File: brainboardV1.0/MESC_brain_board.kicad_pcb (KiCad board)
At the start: 4 copper layers, 90.5 x 68.6 mm, 55 parts, among them J1 Conn_01x18, J12 Conn_01x03, J13 Conn_01x03, J14 SERIAL1, J15 Conn_01x03, J22 Conn_01x01, J24 Conn_01x01, J25 Conn_01x01, Q1 my_BC337, U1 TJA1050T/CM,118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

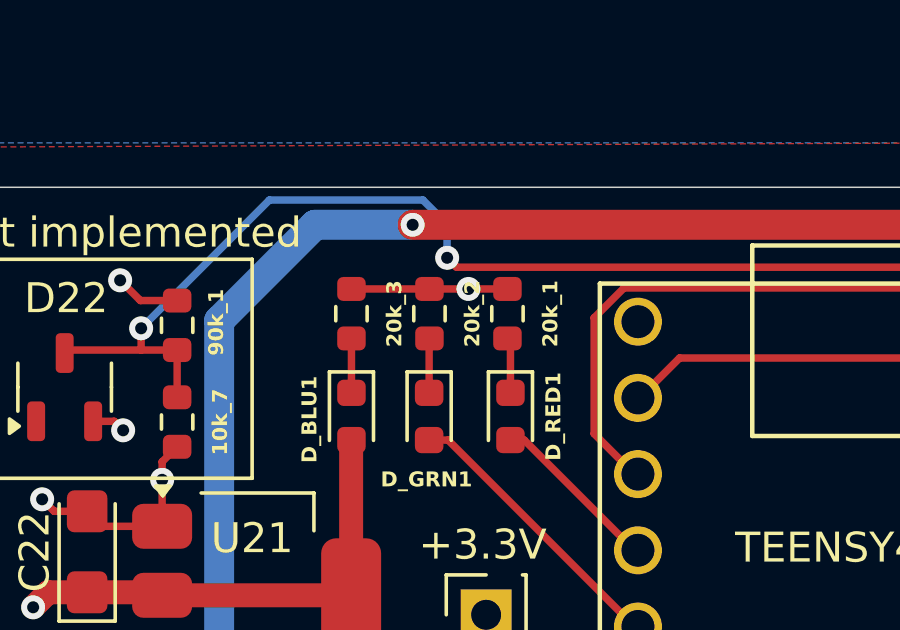
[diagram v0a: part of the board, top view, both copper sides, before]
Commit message: update grn LED resistor
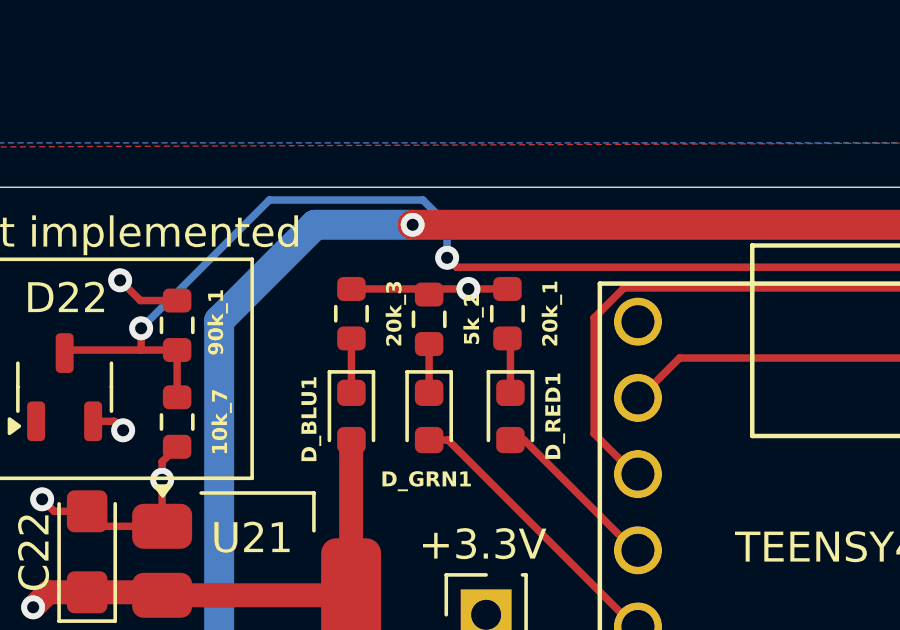
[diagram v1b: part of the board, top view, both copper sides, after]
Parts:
- removed 20k_2: 20k, Resistor_SMD:R_0603_1608Metric
- added 5k_2: 5k, Resistor_SMD:R_0603_1608Metric, F.Cu at (41.1, 19.9)
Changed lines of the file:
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@@
 		)
 	)
-	(footprint "Resistor_SMD:R_0603_1608Metric"
-		(layer "F.Cu")
-		(at 41.11 19.71375 -90)
-		(descr "Resistor SMD 0603 (1608 Metric), square (rectangular) end terminal, IPC_7351 nominal, (Body size source: IPC-SM-782 page 72, https://www.pcb-3d.com/wordpress/wp-content/uploads/ipc-sm-782a_amendment_1_and_2.pdf), generated with kicad-footprint-generator")
-		(tags "resistor")
-		(property "Reference" "20k_2"
-			(at 0 -1.43 90)
-			(layer "F.SilkS")
-			(effects
-				(font
-					(size 0.5 0.5)
-					(thickness 0.1)
-					(bold yes)
-				)
-			)
-		)
-		(property "Value" "20k"
-			(at 0 1.43 90)
-			(layer "F.Fab")
-			(effects
-				(font
-					(size 1 1)
-					(thickness 0.15)
-				)
-			)
-		)
-		(property "Footprint" "Resistor_SMD:R_0603_1608Metric"
-			(at 0 0 -90)
-			(unlocked yes)
-			(layer "F.Fab")
-			(hide yes)
-			(effects
-				(font
-					(size 1.27 1.27)
-					(thickness 0.15)
-				)
-			)
-		)
-		(property "Datasheet" ""
-			(at 0 0 -90)
-			(unlocked yes)
-			(layer "F.Fab")
-			(hide yes)
-			(effects
-				(font
-					(size 1.27 1.27)
-					(thickness 0.15)
-				)
-			)
-		)
-		(property "Description" ""
-			(at 0 0 -90)
-			(unlocked yes)
-			(layer "F.Fab")
-			(hide yes)
-			(effects
-				(font
-					(size 1.27 1.27)
-					(thickness 0.15)
-				)
-			)
-		)
-		(property "LCSC" "C4184"
-			(at 0 0 -90)
-			(unlocked yes)
-			(layer "F.Fab")
-			(hide yes)
-			(effects
-				(font
-					(size 1 1)
-					(thickness 0.15)
-				)
-			)
-		)
-		(property ki_fp_filters "R_*")
-		(sheetname "POWER Sheet")
-		(sheetfile "POWER.kicad_sch")
-		(attr smd)
-		(fp_line
-			(start -0.237258 0.5225)
-			(end 0.237258 0.5225)
-			(stroke
-				(width 0.12)
-				(type solid)
-			)
-			(layer "F.SilkS")
-		)
-		(fp_line
-			(start -0.237258 -0.5225)
-			(end 0.237258 -0.5225)
-			(stroke
-				(width 0.12)
-				(type solid)
-			)
-			(layer "F.SilkS")
-		)
-		(fp_line
-			(start -1.48 0.73)
-			(end -1.48 -0.73)
-			(stroke
-				(width 0.05)
-				(type solid)
-			)
-			(layer "F.CrtYd")
-		)
-		(fp_line
-			(start 1.48 0.73)
-			(end -1.48 0.73)
-			(stroke
-				(width 0.05)
-				(type solid)
-			)
-			(layer "F.CrtYd")
-		)
-		(fp_line
-			(start -1.48 -0.73)
-			(end 1.48 -0.73)
-			(stroke
-				(width 0.05)
-				(type solid)
-			)
-			(layer "F.CrtYd")
-		)
-		(fp_line
-			(start 1.48 -0.73)
-			(end 1.48 0.73)
-			(stroke
-				(width 0.05)
-				(type solid)
-			)
-			(layer "F.CrtYd")
-		)
-		(fp_line
-			(start -0.8 0.4125)
-			(end -0.8 -0.4125)
-			(stroke
-				(width 0.1)
-				(type solid)
-			)
-			(layer "F.Fab")
-		)
-		(fp_line
-			(start 0.8 0.4125)
-			(end -0.8 0.4125)
-			(stroke
-				(width 0.1)
-				(type solid)
-			)
-			(layer "F.Fab")
-		)
-		(fp_line
-			(start -0.8 -0.4125)
-			(end 0.8 -0.4125)
-			(stroke
-				(width 0.1)
-				(type solid)
-			)
-			(layer "F.Fab")
-		)
-		(fp_line
-			(start 0.8 -0.4125)
-			(end 0.8 0.4125)
-			(stroke
-				(width 0.1)
-				(type solid)
-			)
-			(layer "F.Fab")
-		)
-		(fp_text user "${REFERENCE}"
-			(at 0 0 90)
-			(layer "F.Fab")
-			(effects
-				(font
-					(size 0.4 0.4)
-					(thickness 0.06)
-				)
-			)
-		)
-		(pad "1" smd roundrect
-			(at -0.825 0 270)
-			(size 0.8 0.95)
-			(layers "F.Cu" "F.Paste" "F.Mask")
-			(roundrect_rratio 0.25)
-			(net 1 "GND")
-			(pintype "passive")
-		)
-		(pad "2" smd roundrect
-			(at 0.825 0 270)
-			(size 0.8 0.95)
-			(layers "F.Cu" "F.Paste" "F.Mask")
-			(roundrect_rratio 0.25)
-			(net 85 "Net-(D_GRN1-K)")
-			(pintype "passive")
-		)
-		(model "${KICAD8_3DMODEL_DIR}/Resistor_SMD.3dshapes/R_0603_1608Metric.wrl"
-			(offset
-				(xyz 0 0 0)
-			)
-			(scale
-				(xyz 1 1 1)
-			)
-			(rotate
-				(xyz 0 0 0)
-			)
-		)
-	)
 	(footprint "Converter_DCDC:my_buck_boost"
 		(layer "F.Cu")
@@
 			(offset
 				(xyz 0 0 0)
+			)
+			(scale
+				(xyz 1 1 1)
+			)
+			(rotate
+				(xyz 0 0 0)
+			)
+		)
+	)
+	(footprint "Resistor_SMD:R_0603_1608Metric"
+		(layer "F.Cu")
+		(at 41.1 19.9 -90)
+		(descr "Resistor SMD 0603 (1608 Metric), square (rectangular) end terminal, IPC_7351 nominal, (Body size source: IPC-SM-782 page 72, https://www.pcb-3d.com/wordpress/wp-content/uploads/ipc-sm-782a_amendment_1_and_2.pdf), generated with kicad-footprint-generator")
+		(tags "resistor")
+		(property "Reference" "5k_2"
+			(at 0 -1.43 90)
+			(layer "F.SilkS")
+			(effects
+				(font
+					(size 0.5 0.5)
+					(thickness 0.1)
+					(bold yes)
+				)
+			)
+		)
+		(property "Value" "5k"
+			(at 0 1.43 90)
+			(layer "F.Fab")
+			(hide yes)
+			(effects
+				(font
+					(size 1 1)
+					(thickness 0.15)
+				)
+			)
+		)
+		(property "Footprint" "Resistor_SMD:R_0603_1608Metric"
+			(at 0 0 -90)
+			(unlocked yes)
+			(layer "F.Fab")
+			(hide yes)
+			(effects
+				(font
+					(size 1.27 1.27)
+					(thickness 0.15)
+				)
+			)
+		)
+		(property "Datasheet" ""
+			(at 0 0 -90)
+			(unlocked yes)
+			(layer "F.Fab")
+			(hide yes)
+			(effects
+				(font
+					(size 1.27 1.27)
+					(thickness 0.15)
+				)
+			)
+		)
+		(property "Description" ""
+			(at 0 0 -90)
+			(unlocked yes)
+			(layer "F.Fab")
+			(hide yes)
+			(effects
+				(font
+					(size 1.27 1.27)
+					(thickness 0.15)
+				)
+			)
+		)
+		(property "LCSC" "C4184"
+			(at 0 0 -90)
+			(unlocked yes)
+			(layer "F.Fab")
+			(hide yes)
+			(effects
+				(font
+					(size 1 1)
+					(thickness 0.15)
+				)
+			)
+		)
+		(property ki_fp_filters "R_*")
+		(sheetname "POWER Sheet")
+		(sheetfile "POWER.kicad_sch")
+		(attr smd)
+		(fp_line
+			(start -0.237258 0.5225)
+			(end 0.237258 0.5225)
+			(stroke
+				(width 0.12)
+				(type solid)
+			)
+			(layer "F.SilkS")
+		)
+		(fp_line
+			(start -0.237258 -0.5225)
+			(end 0.237258 -0.5225)
+			(stroke
+				(width 0.12)
+				(type solid)
+			)
+			(layer "F.SilkS")
+		)
+		(fp_line
+			(start -1.48 0.73)
+			(end -1.48 -0.73)
+			(stroke
+				(width 0.05)
+				(type solid)
+			)
+			(layer "F.CrtYd")
+		)
+		(fp_line
+			(start 1.48 0.73)
+			(end -1.48 0.73)
+			(stroke
+				(width 0.05)
+				(type solid)
+			)
+			(layer "F.CrtYd")
+		)
+		(fp_line
+			(start -1.48 -0.73)
+			(end 1.48 -0.73)
+			(stroke
+				(width 0.05)
+				(type solid)
+			)
+			(layer "F.CrtYd")
+		)
+		(fp_line
+			(start 1.48 -0.73)
+			(end 1.48 0.73)
+			(stroke
+				(width 0.05)
+				(type solid)
+			)
+			(layer "F.CrtYd")
+		)
+		(fp_line
+			(start -0.8 0.4125)
+			(end -0.8 -0.4125)
+			(stroke
+				(width 0.1)
+				(type solid)
+			)
+			(layer "F.Fab")
+		)
+		(fp_line
+			(start 0.8 0.4125)
+			(end -0.8 0.4125)
+			(stroke
+				(width 0.1)
+				(type solid)
+			)
+			(layer "F.Fab")
+		)
+		(fp_line
+			(start -0.8 -0.4125)
+			(end 0.8 -0.4125)
+			(stroke
+				(width 0.1)
+				(type solid)
+			)
+			(layer "F.Fab")
+		)
+		(fp_line
+			(start 0.8 -0.4125)
+			(end 0.8 0.4125)
+			(stroke
+				(width 0.1)
+				(type solid)
+			)
+			(layer "F.Fab")
+		)
+		(fp_text user "${REFERENCE}"
+			(at 0 0 0)
+			(layer "F.Fab")
+			(effects
+				(font
+					(size 0.4 0.4)
+					(thickness 0.06)
+				)
+			)
+		)
+		(pad "1" smd roundrect
+			(at -0.825 0 270)
+			(size 0.8 0.95)
+			(layers "F.Cu" "F.Paste" "F.Mask")
+			(roundrect_rratio 0.25)
+			(net 1 "GND")
+			(pintype "passive")
+		)
+		(pad "2" smd roundrect
+			(at 0.825 0 270)
+			(size 0.8 0.95)
+			(layers "F.Cu" "F.Paste" "F.Mask")
+			(roundrect_rratio 0.25)
+			(net 85 "Net-(D_GRN1-K)")
+			(pintype "passive")
+		)
+		(model "${KICAD8_3DMODEL_DIR}/Resistor_SMD.3dshapes/R_0603_1608Metric.wrl"
+			(offset
+				(xyz 0 0 0)
